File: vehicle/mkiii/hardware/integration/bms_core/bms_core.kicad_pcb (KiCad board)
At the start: 4 copper layers, 101.4 x 25.1 mm, 88 parts, among them J2 CONN_02x03, J3 MicroFit_RA_2, J4 J_Programming_Pin_Header, J5 J_PCIe_x1, K1 Relay_G5Q-1A4-DC5, Q1 SSM3K333R, T1 HM2112ZNLT, U10 STM32G441KBT6, U11 MCP2561-E_SN, U3 LTC6820HMS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

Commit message: Changes according to feedback
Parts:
- added C1: C_0.1uF_16V, OEM:C_0603_1608Metric, F.Cu at (185.2, 102.2)
- added U1: MCP6001, Package_TO_SOT_SMD:SOT-353_SC-70-5, F.Cu at (185.2, 104.7)
- R5: value R_120_DNP -> R_120; footprint OEM:R_0603 -> OEM:R_0603_1608Metric
- moved C9 66.7 mm to (181.9, 102.5)
- moved U4 66.5 mm to (182.0, 104.8)
- moved R15 66.2 mm to (179.6, 104.7)
- moved C13 65.9 mm to (175.7, 107.1)
- moved C14 65.9 mm to (144.2, 112.2)
- moved C15 65.9 mm to (136.7, 112.2)
- moved C16 65.9 mm to (144.9, 98.2)
- moved C17 65.9 mm to (134.4, 106.7)
- moved C18 65.9 mm to (135.9, 108.7)
- moved C19 65.9 mm to (147.2, 100.7)
- moved C20 65.9 mm to (147.2, 104.7)
- moved C21 65.9 mm to (136.2, 99.7)
- moved C22 65.9 mm to (150.9, 97.2)
- moved CANH 65.9 mm to (159.4, 110.7)
- moved CANL 65.9 mm to (154.9, 110.7)
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- renumbered V_GND to VGND
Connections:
- J5 pad B8: /VOUT_CURRENT_SENSE -> Net-(J5-io_5)
- U10 pad 20: /VOUT_CURRENT_SENSE -> unconnected-(U10-(TIM2_CH4/USART1_RX/TIM17_BKIN/GPIO_EXTI10)PA10-Pad20)
- U10 pad 9: unconnected-(U10-(USART2_CK/TIM3_CH2/GPIO_EXTI4/ADC2_IN17)PA4*-Pad9) -> /VOUT_CURRENT_SENSE
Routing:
- net /VOUT_CURRENT_SENSE: track 61.3 -> 48.5 mm
- net Net-(J5-io_5): track 0.00 -> 7.20 mm
- net GND: track 78.7 -> 85.0 mm, vias 32 -> 33
- net +5V: track 46.0 -> 49.2 mm, vias 13 -> 15
- net /BSPD Current Sensor Trigger/CURRENT_TRIP: track 4.51 -> 6.06 mm
- net Net-(U4--): track 6.28 -> 5.45 mm

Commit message: Final tweaks
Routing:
- net Net-(U10-PF0-OSC_IN): track 12.0 -> 8.36 mm
- net GND: track 85.0 -> 83.0 mm
- net /FAN_PWM: vias 2 -> 0

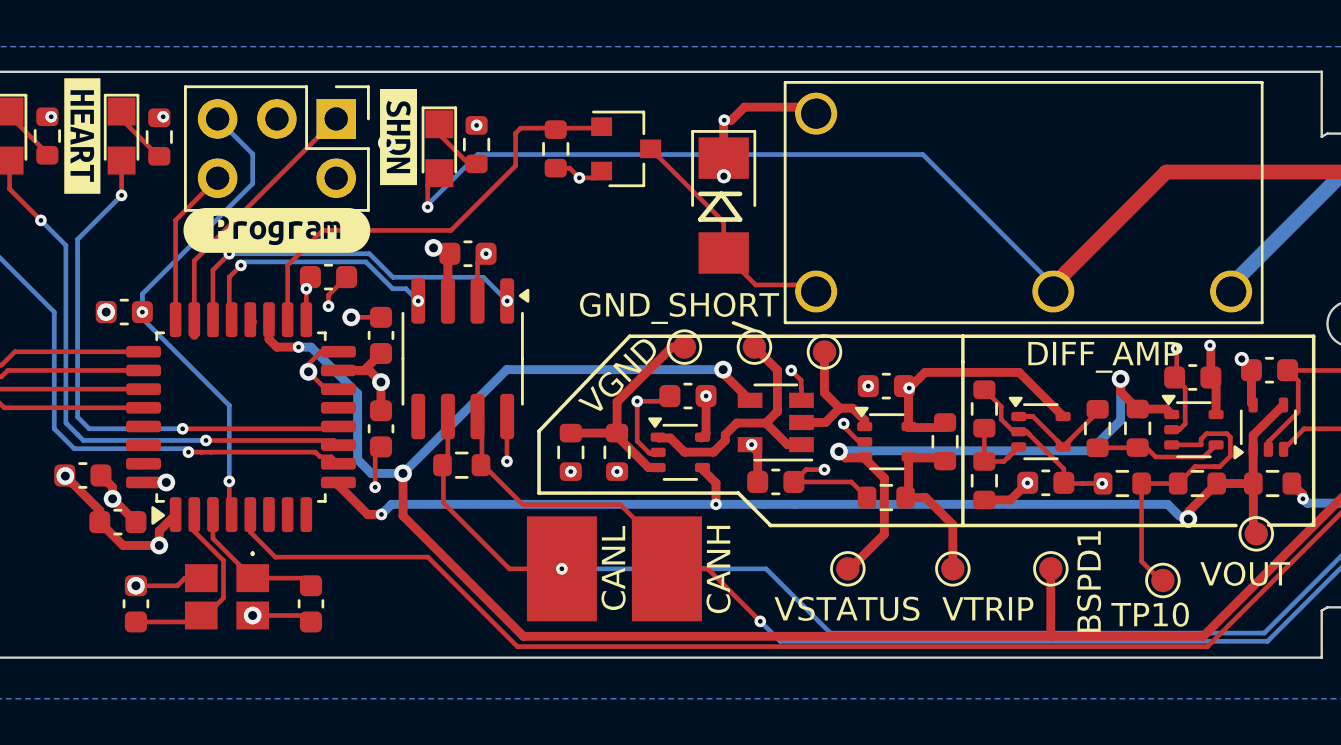
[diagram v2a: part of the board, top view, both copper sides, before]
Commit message: Schematics and PCB Layout are Preliminarily Approved - DRC and ERC results are good.
Changes:
- Updated Title Block Info on Schematics
- Modified Silkscreen Text for test point
- Rerouted NRST trace
- Added OEM Logo to PCB Layout

Great work Akil :)
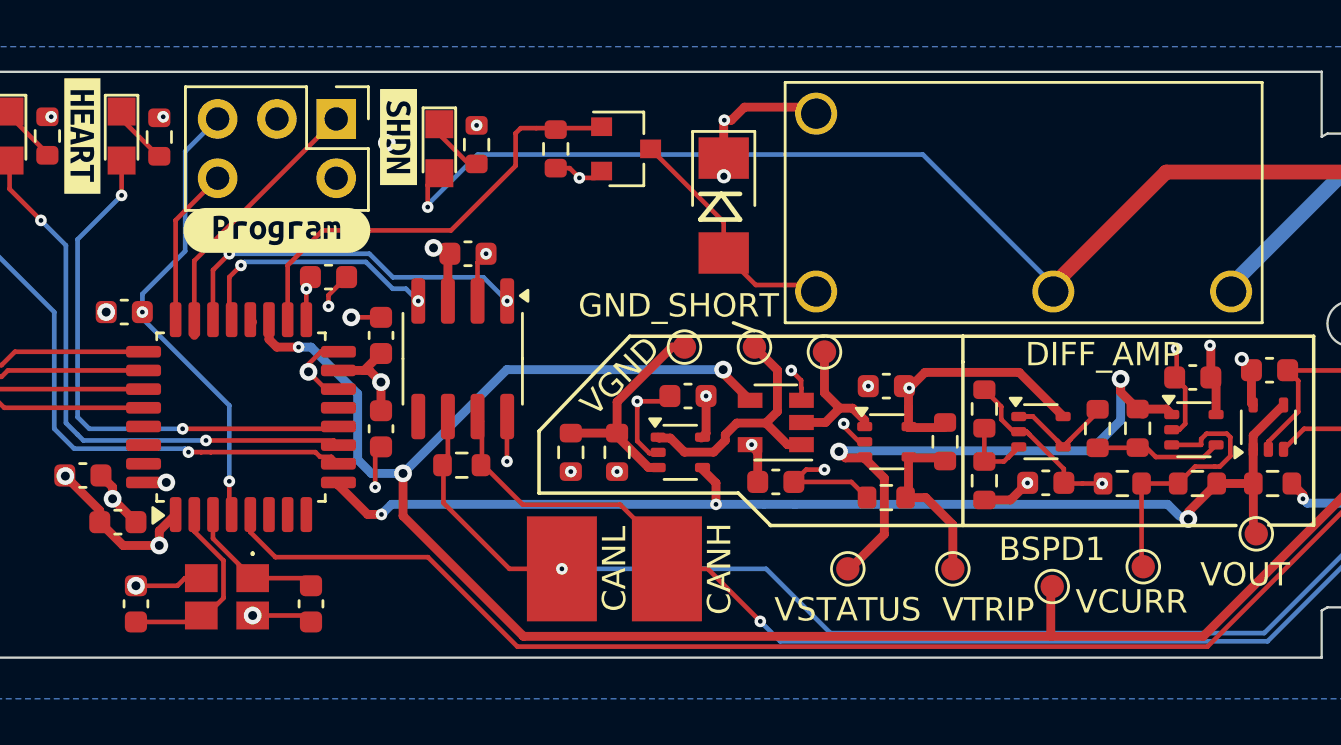
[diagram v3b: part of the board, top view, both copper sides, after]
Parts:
- removed G***: LOGO, Toad:Toad
- removed kibuzzard-673AE93C: G***, kibuzzard-673AE93C
- removed kibuzzard-673AE955: G***, kibuzzard-673AE955
- removed kibuzzard-673AE966: G***, kibuzzard-673AE966
- added kibuzzard-69802617: G***, kibuzzard-69802617, B.Cu at (172.8, 105.7)
- added kibuzzard-698026CF: G***, kibuzzard-698026CF, B.Cu at (169.6, 108.5)
- added kibuzzard-69802858: G***, kibuzzard-69802858, B.Cu at (169.2, 111.4)
- moved REF** 132.5 mm to (181.5, 108.5)
- moved VCURR 1.03 mm to (179.8, 110.7)
- moved BSPD1 0.76 mm to (175.9, 111.5)
- renumbered TP10 to VCURR
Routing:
- net /NRST: track 22.1 -> 20.8 mm
- net Net-(U4-+): track 12.6 -> 11.6 mm
- net /BSPD_CURRENT_THRESH: track 83.8 -> 83.2 mm

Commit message: Make changes from feedback
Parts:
- added R2: R_5.1k, OEM:R_0603_1608Metric, F.Cu at (148.5, 111.5)
- added R4: R_10k, OEM:R_0603_1608Metric, F.Cu at (146.7, 109.5)
- renumbered VCURR to VOUT
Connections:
- U10 pad 9: /VOUT_CURRENT_SENSE -> Net-(U10-(USART2_CK/TIM3_CH2/GPIO_EXTI4/ADC2_IN17)PA4*)
- U4 pad 3: Net-(U4-+) -> /VOUT_CURRENT_SENSE
- VOUT pad 1: Net-(U4-+) -> /VOUT_CURRENT_SENSE
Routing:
- net Net-(U10-(USART2_CK/TIM3_CH2/GPIO_EXTI4/ADC2_IN17)PA4*): track 0.00 -> 5.54 mm
- net /VOUT_CURRENT_SENSE: track 48.5 -> 45.9 mm
- net /CANL: track 51.0 -> 51.6 mm
- net +5V: track 49.2 -> 49.8 mm
- net GND: vias 33 -> 34

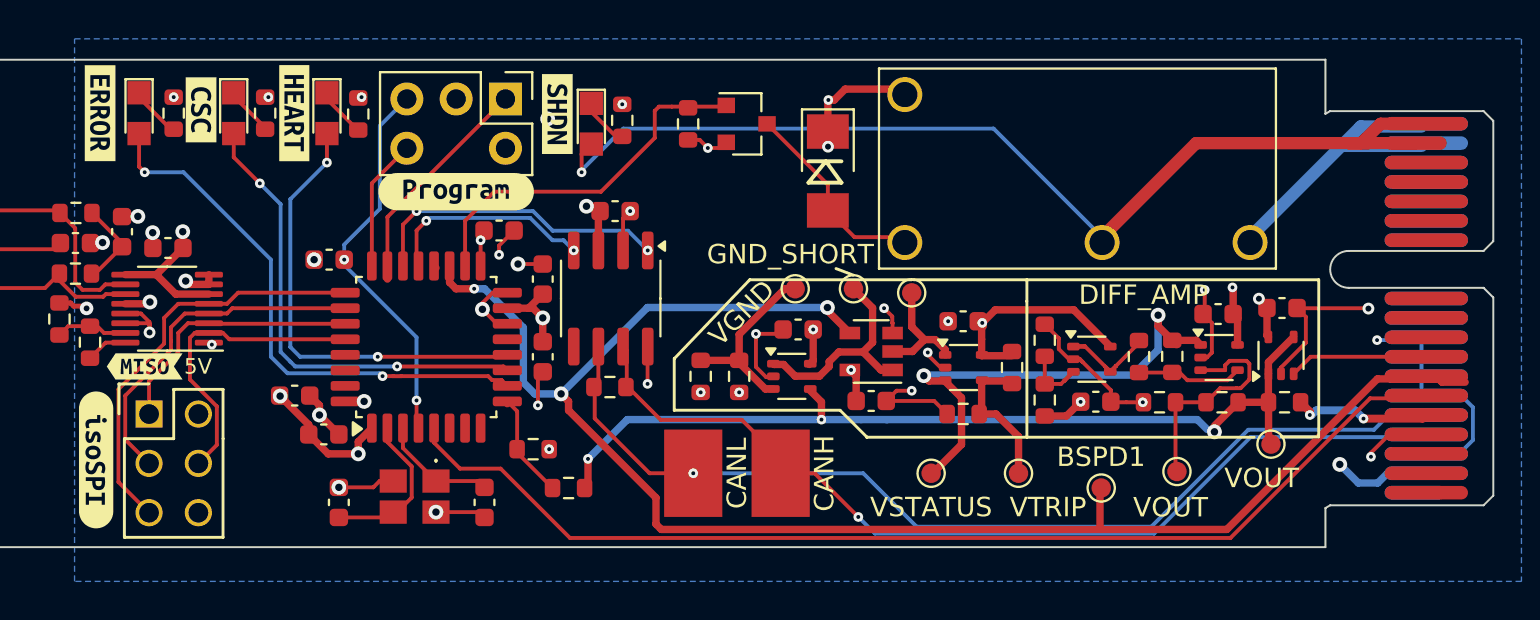
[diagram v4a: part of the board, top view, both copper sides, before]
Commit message: Added Subteam Logo, Production Files, and readded isoSPI debugging header.
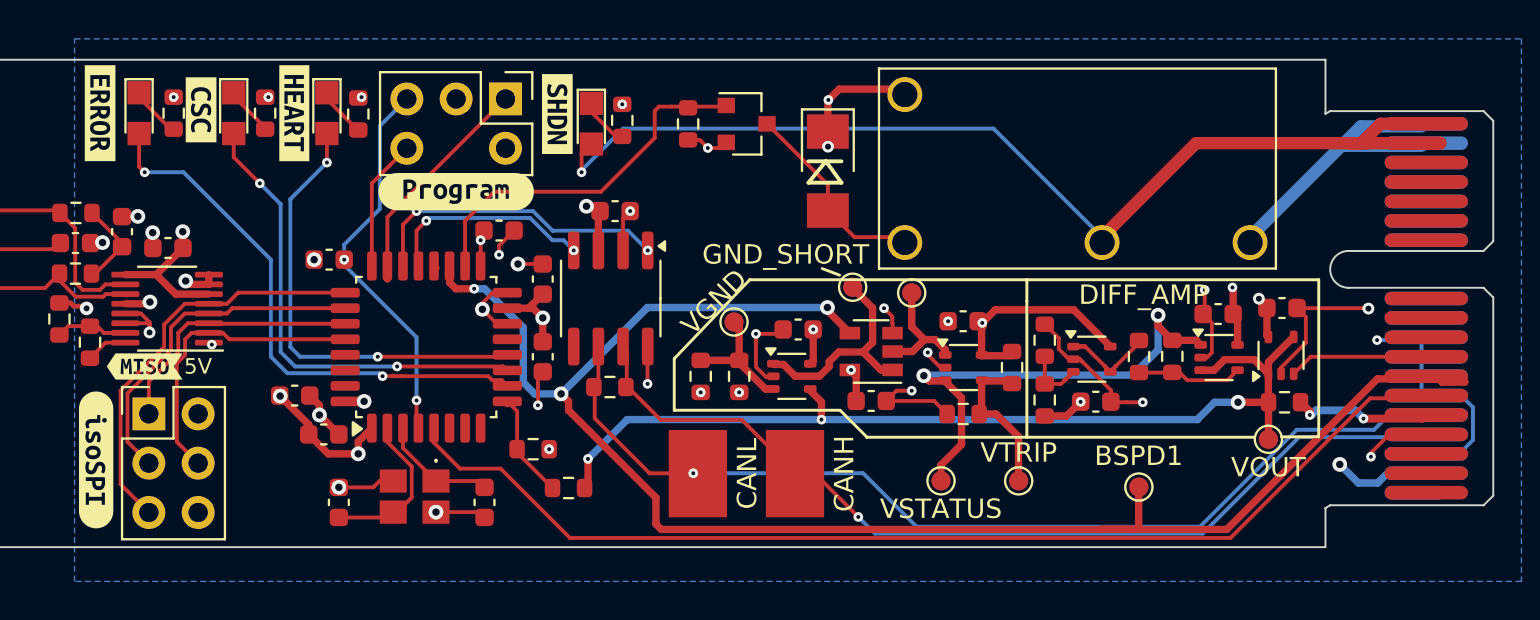
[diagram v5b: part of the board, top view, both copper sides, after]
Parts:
- removed J2: CONN_02x03, footprints:Pin_Header_Straight_2x03
- removed R13, R14: R_10K, OEM:R_0603
- removed the VOUT at (179.8, 110.7)
- removed the VOUT at (184.7, 109.2)
- added G***: LOGO, LOGO, B.Cu at (156.1, 98.3)
- added J1: isoSPI Header, Connector_PinHeader_2.54mm:PinHeader_2x03_P2.54mm_Vertical, F.Cu at (126.9, 107.7)
- added VOUT: VOUT, TestPoint:TestPoint_Pad_D1.0mm, F.Cu at (184.5, 109.0)
- C18: value C_0.1uF_16V -> C_4.7uF_25V
- C19: value C_0.1uF_16V -> C_10nF_50V
- C20: value C_0.1uF_16V -> C_1uF_25V
- moved VGND 3.59 mm to (157.0, 103.0), turned to 45 degrees
- moved BSPD1 1.94 mm to (177.9, 111.5)
- moved CANH 0.74 mm to (160.2, 110.8)
- moved VSTATUS 0.64 mm to (167.7, 111.1), turned to 180 degrees
- moved VTRIP 0.39 mm to (171.7, 111.1)
- moved CANL 0.24 mm to (155.2, 110.8)
- moved GND_SHORT 0.09 mm to (163.1, 101.2)
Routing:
- net Net-(U4-+): track 11.6 -> 0.00 mm
- net /VOUT_CURRENT_SENSE: track 45.9 -> 49.9 mm
- net /BSPD Current Sensor Trigger/V_GND_THRESHOLD: track 9.62 -> 6.51 mm
- net /BSPD_CURRENT_THRESH: track 83.2 -> 85.2 mm
- net +3V3: vias 6 -> 5

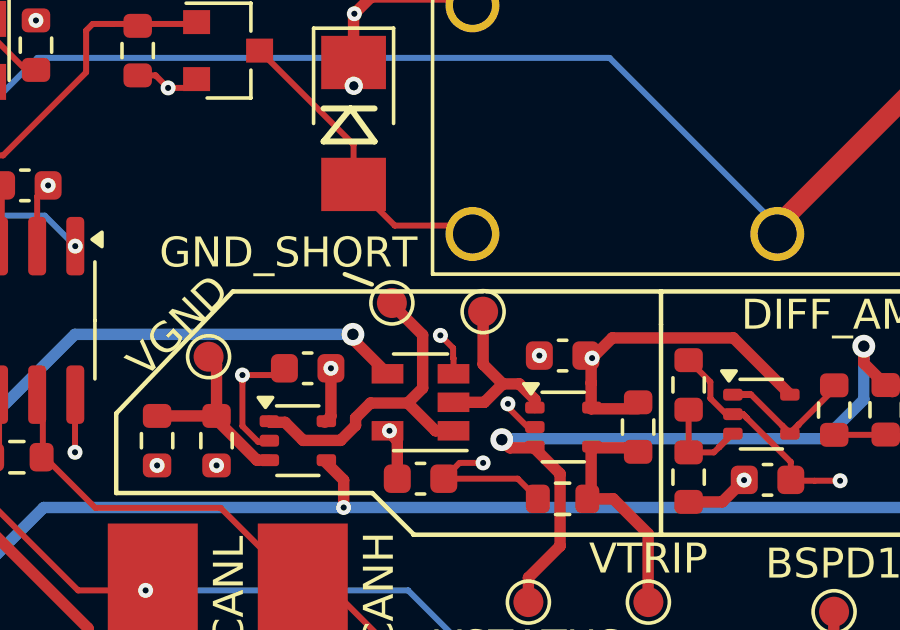
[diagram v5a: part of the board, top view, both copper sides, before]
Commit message: Fixed minor silkscreen issue (Added CTRIP label) and updated production files.
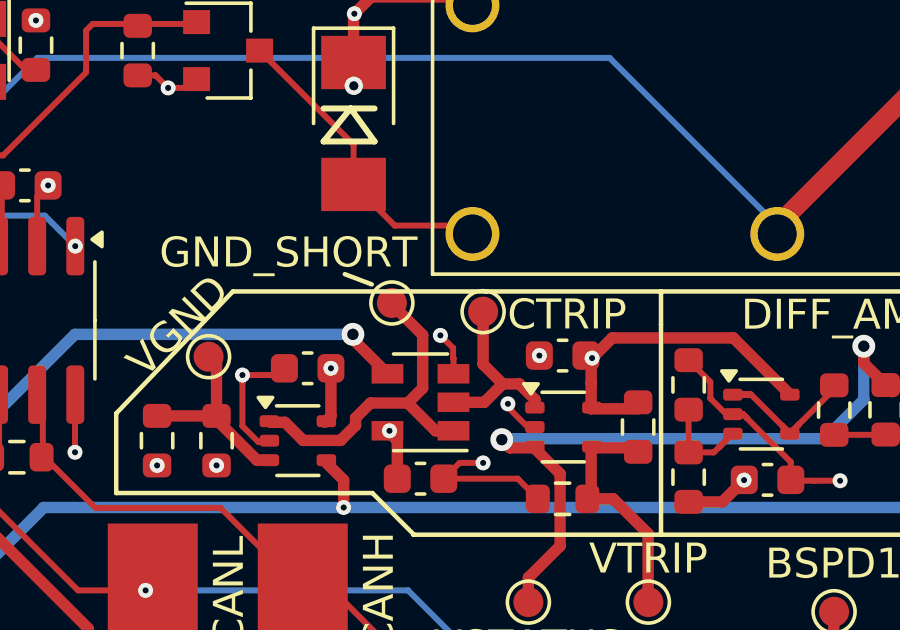
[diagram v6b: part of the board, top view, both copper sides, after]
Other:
- board text added: "CTRIP"
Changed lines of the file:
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@@
 	)
 	(gr_line
-		(start 166.171 100.7754)
+		(start 166.2728 100.7754)
 		(end 157.8292 100.7754)
 		(stroke
@@
 		)
 	)
+	(gr_text "CTRIP"
+		(at 166.98 102.13 0)
+		(layer "F.SilkS")
+		(effects
+			(font
+				(size 1 1)
+				(thickness 0.15)
+			)
+			(justify left bottom)
+		)
+	)
